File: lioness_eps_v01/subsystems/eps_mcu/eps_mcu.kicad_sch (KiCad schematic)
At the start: 51 parts, among them J1 10103594-0001LF, J2 TSW-126-07-L-D, J3 SM03B-SRSS-TB(LF)(SN), J4 TSW-126-07-L-D, SW1 434133025816, U1 W25Q128JVSIQ, U2 W25Q128JVSIQ, U3 NCP1117ST33T3G, U4 RP2350B, U5 MAX706RESA+T, X1 12MHz

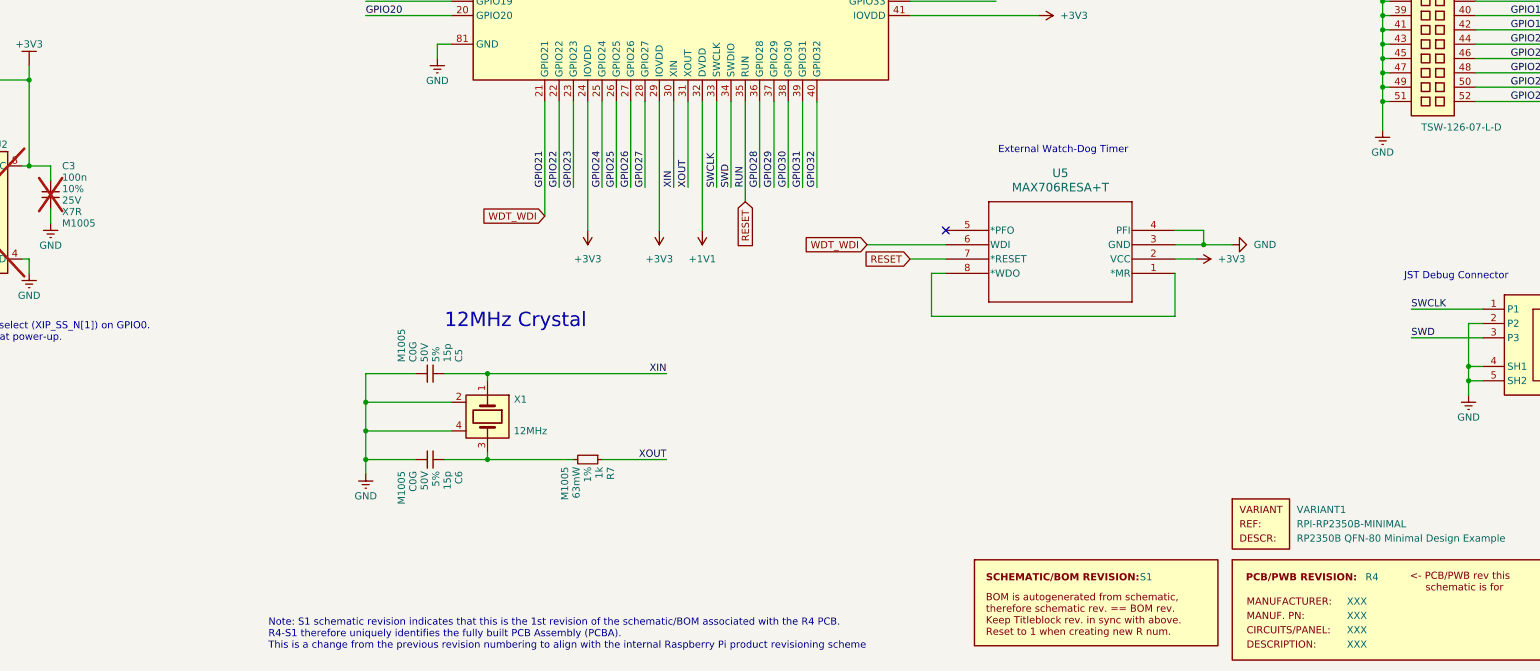
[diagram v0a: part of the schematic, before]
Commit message: added status LED and debug connections
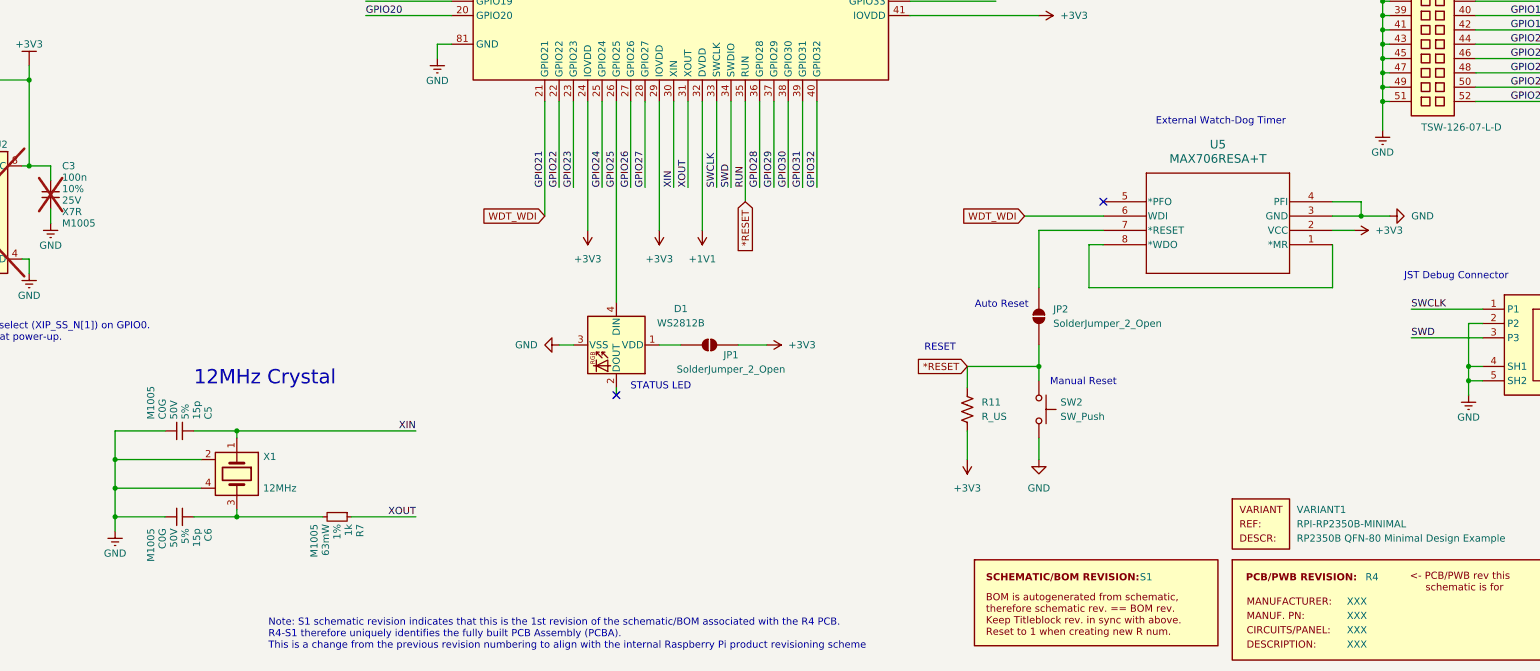
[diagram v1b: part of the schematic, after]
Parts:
- added D1: WS2812B, LED_SMD:LED_WS2812B_PLCC4_5.0x5.0mm_P3.2mm, symbol LED:WS2812B
- added JP1: SolderJumper_2_Open, Package_LCC:PLCC-84_29.3x29.3mm_P1.27mm, symbol Jumper:SolderJumper_2_Open
- added JP2: SolderJumper_2_Open, symbol Jumper:SolderJumper_2_Open
- added R11: R_US, Package_DIP:DIP-8_W7.62mm, symbol Device:R_US
- added SW2: SW_Push, Button_Switch_SMD:SW_Push_1P1T_NO_CK_KMR2, symbol Switch:SW_Push
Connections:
- net +3V3: now also JP1.2 (B), R11.2
- net GND: now also D1.3 (VSS), SW2.2
- net GPIO25: now also D1.4 (DIN)
- net RESET: no longer names the net of U5.7 (*RESET)
- net RESET: now also JP2.1 (A); no longer U4.35 (RUN)
- new net: D1.1 (VDD), JP1.1 (A)
- new net *RESET: JP2.2 (B), R11.1, SW2.1, U4.35 (RUN)
- no-connect marks 2 -> 3
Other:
- note added: "Auto Reset"
- note added: "Manual Reset"
- note added: "RESET"
- note added: "STATUS LED"
- moved on the sheet: C5, C6, R7, U5, X1

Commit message: added picolocks and debugging connections
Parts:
- added D2: LED, symbol Device:LED
- added J5: RBF, Connector_Molex:Molex_Pico-Lock_504050-0291_1x02-1MP_P1.50mm_Horizontal, symbol Connector_Generic:Conn_01x02
- added J6, J8: Foot0, Connector_Molex:Molex_Pico-Lock_504050-0291_1x02-1MP_P1.50mm_Horizontal, symbol Connector_Generic:Conn_01x02
- added J7, J9: Foot1, Connector_Molex:Molex_Pico-Lock_504050-0291_1x02-1MP_P1.50mm_Horizontal, symbol Connector_Generic:Conn_01x02
- added R12: 10k, Package_DIP:DIP-8_W7.62mm, symbol Device:R_US
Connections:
- net GND: now also D2.1 (K)
- net VBUS: now also J5.1 (Pin_1); no longer C1.1, J1.1 (VCC), U3.3 (IN)
- new net: J6.1 (Pin_1), J7.2 (Pin_2)
- new net: J8.1 (Pin_1), J9.2 (Pin_2)
- new net: D2.2 (A), R12.2
- new net VBatt: J6.2 (Pin_2), J8.2 (Pin_2)
- new net VBatt1: J5.2 (Pin_2), J7.1 (Pin_1), J9.1 (Pin_1)
- new net VUSB: C1.1, J1.1 (VCC), R12.1, U3.3 (IN)
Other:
- note added: "2 Pin Picolocks"
- note added: "Debug Connections"
- note added: "Primary Flash (16MB)"
- note added: "Secondary Flash/PSRAM (+16MB)"
- note added: "USB Connector"
- note removed: "Power (REDO, not USB)"
- note removed: "Primary Flash"
- note removed: "Secondary Flash/PSRAM"
- moved on the sheet: C1, C12, C13, C15, C16, C18, C19, C2, C20, C21, C22, C3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
